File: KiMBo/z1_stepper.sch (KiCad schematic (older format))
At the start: 23 parts, among them U21 TMC2130

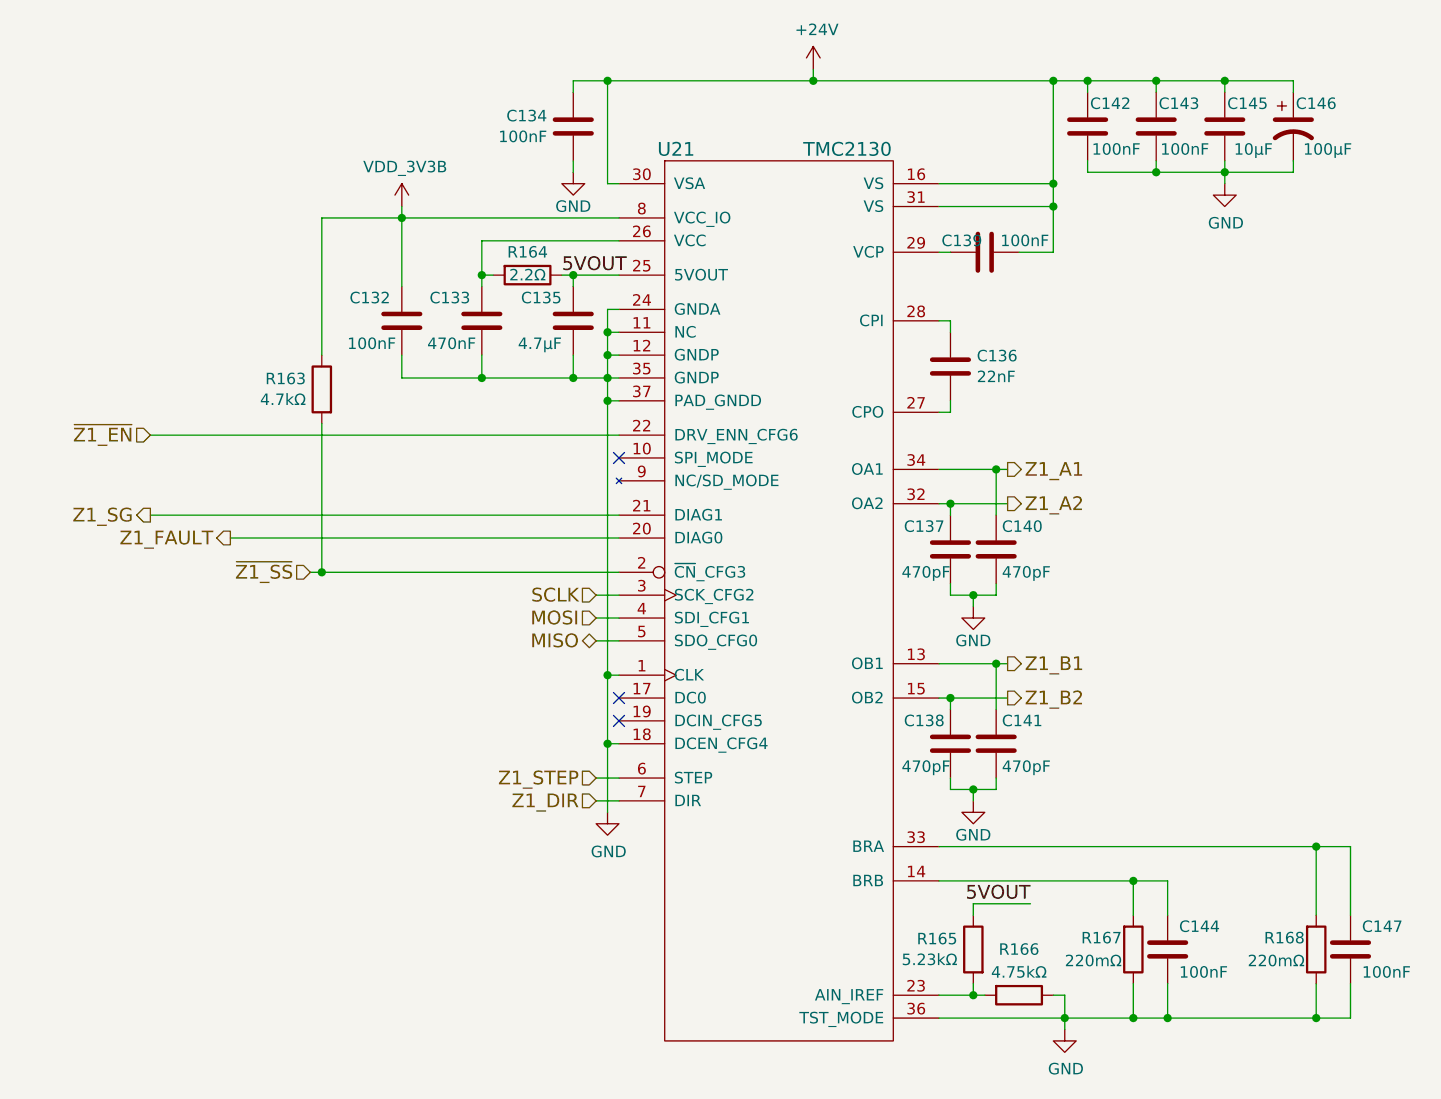
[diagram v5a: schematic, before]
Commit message: Remove HDMI from the schematic
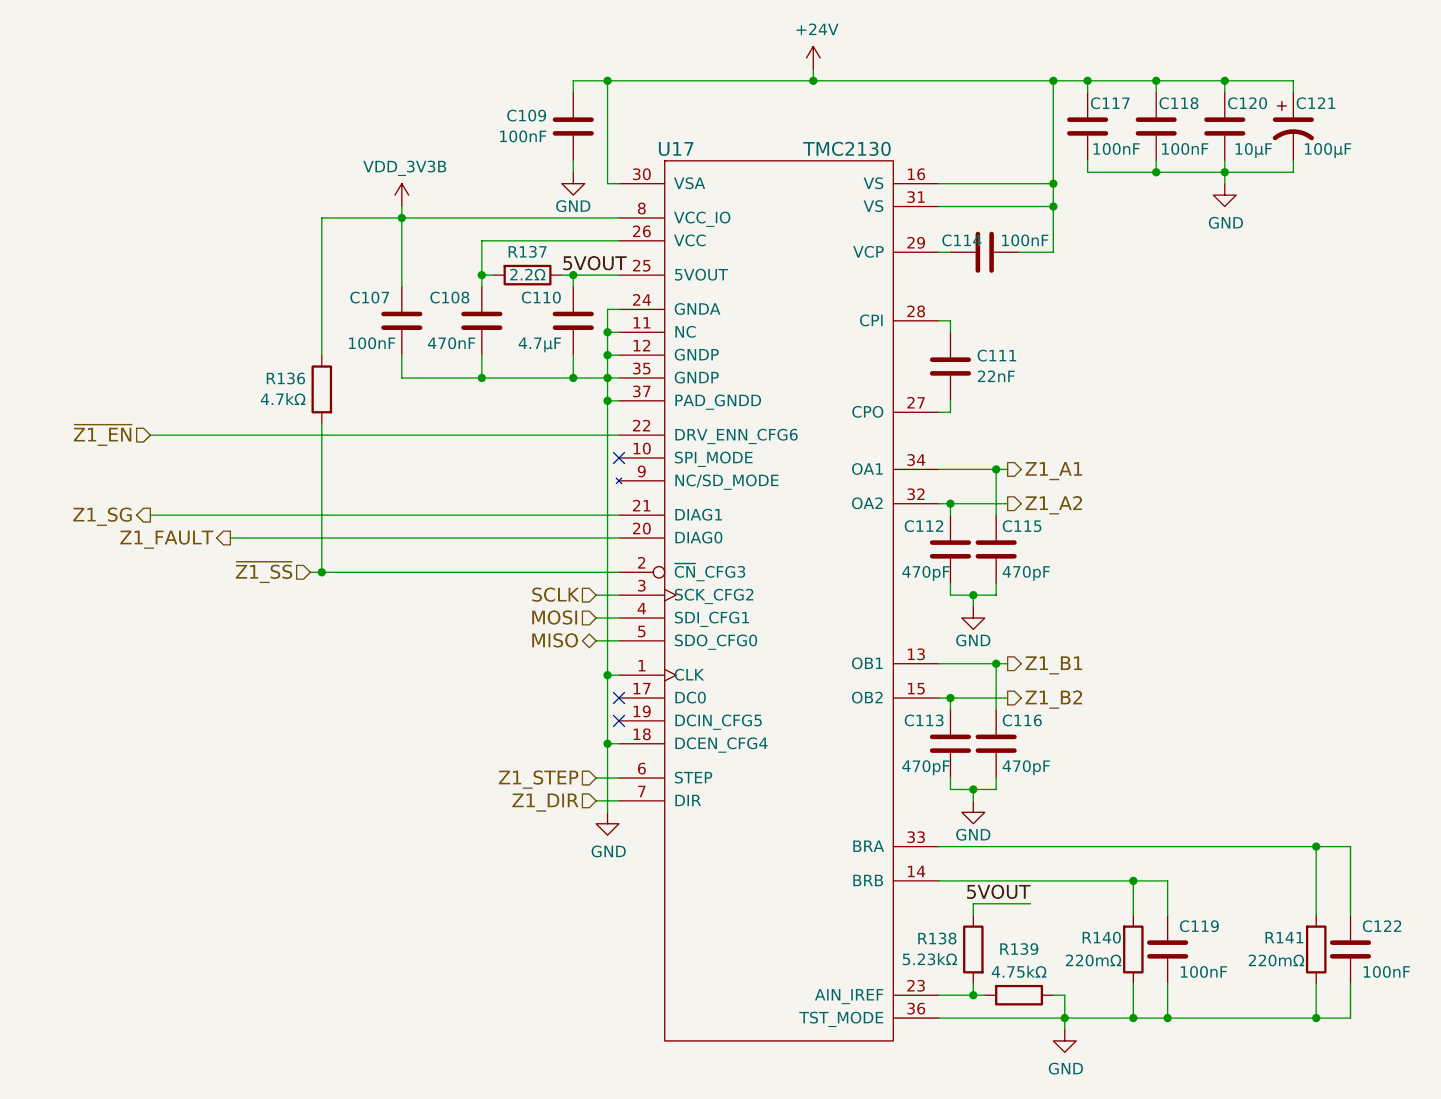
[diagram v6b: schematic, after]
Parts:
- renumbered C132 to C107, C133 to C108, C134 to C109, C135 to C110, C136 to C111, C137 to C112, C138 to C113, C139 to C114, C140 to C115, C141 to C116, C142 to C117, C143 to C118, C144 to C119, C145 to C120, C146 to C121, C147 to C122, R163 to R136, R164 to R137, R165 to R138, R166 to R139, R167 to R140, R168 to R141, U21 to U17
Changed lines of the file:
@@
 $Descr A3 16535 11693
 encoding utf-8
-Sheet 19 26
+Sheet 19 25
 Title ""
 Date ""
@@
 Z1_SG
 $Comp
-L C C134
+L C C109
 U 1 1 58C0CFD1
 P 7400 3050
-F 0 "C134" H 7286 3004 50  0000 R CNN
+F 0 "C109" H 7286 3004 50  0000 R CNN
 F 1 "100nF" H 7286 3095 50  0000 R CNN
 F 2 "Capacitors_SMD:C_0603" H 7438 2900 50  0001 C CNN
@@
 $EndComp
 $Comp
-L C C139
+L C C114
 U 1 1 58C0CFD8
 P 9200 3600
-F 0 "C139" V 9150 3500 50  0000 C CNN
+F 0 "C114" V 9150 3500 50  0000 C CNN
 F 1 "100nF" V 9150 3775 50  0000 C CNN
 F 2 "Capacitors_SMD:C_0603" H 9238 3450 50  0001 C CNN
@@
 $EndComp
 $Comp
-L CP1 C146
+L CP1 C121
 U 1 1 58C0CFDF
 P 10550 3050
-F 0 "C146" H 10650 3150 50  0000 C CNN
+F 0 "C121" H 10650 3150 50  0000 C CNN
 F 1 "100μF" H 10700 2950 50  0000 C CNN
 F 2 "Capacitors_SMD:c_elec_8x10" H 10550 3050 50  0001 C CNN
@@
 $EndComp
 $Comp
-L C C142
+L C C117
 U 1 1 58C0CFE6
 P 9650 3050
-F 0 "C142" H 9550 3150 50  0000 C CNN
+F 0 "C117" H 9550 3150 50  0000 C CNN
 F 1 "100nF" H 9525 2950 50  0000 C CNN
 F 2 "Capacitors_SMD:C_0603" H 9688 2900 50  0001 C CNN
@@
 $EndComp
 $Comp
-L GND #PWR0224
+L GND #PWR0193
 U 1 1 58C0CFED
 P 7400 3250
-F 0 "#PWR0224" H 7400 3000 50  0001 C CNN
+F 0 "#PWR0193" H 7400 3000 50  0001 C CNN
 F 1 "GND" H 7400 3100 50  0000 C CNN
 F 2 "" H 7400 3250 50  0000 C CNN
@@
 $EndComp
 $Comp
-L C C143
+L C C118
 U 1 1 58C0CFF3
 P 9950 3050
-F 0 "C143" H 9850 3150 50  0000 C CNN
+F 0 "C118" H 9850 3150 50  0000 C CNN
 F 1 "100nF" H 9825 2950 50  0000 C CNN
 F 2 "Capacitors_SMD:C_0603" H 9988 2900 50  0001 C CNN
@@
 $EndComp
 $Comp
-L GND #PWR0225
+L GND #PWR0194
 U 1 1 58C0CFFA
 P 10250 3300
-F 0 "#PWR0225" H 10250 3050 50  0001 C CNN
+F 0 "#PWR0194" H 10250 3050 50  0001 C CNN
 F 1 "GND" H 10255 3127 50  0000 C CNN
 F 2 "" H 10250 3300 50  0000 C CNN
@@
 $EndComp
 $Comp
-L +24V #PWR0226
+L +24V #PWR0195
 U 1 1 58C0D000
 P 8450 2800
-F 0 "#PWR0226" H 8450 2650 50  0001 C CNN
+F 0 "#PWR0195" H 8450 2650 50  0001 C CNN
 F 1 "+24V" H 8465 2973 50  0000 C CNN
 F 2 "" H 8450 2800 50  0000 C CNN
@@
 $EndComp
 $Comp
-L C C136
+L C C111
 U 1 1 58C0D006
 P 9050 4100
-F 0 "C136" H 9165 4146 50  0000 L CNN
+F 0 "C111" H 9165 4146 50  0000 L CNN
 F 1 "22nF" H 9165 4055 50  0000 L CNN
 F 2 "Capacitors_SMD:C_0603" H 9088 3950 50  0001 C CNN
@@
 $EndComp
 $Comp
-L R R168
+L R R141
 U 1 1 58C0D00D
 P 10650 6650
-F 0 "R168" H 10600 6600 50  0000 R CNN
+F 0 "R141" H 10600 6600 50  0000 R CNN
 F 1 "220mΩ" H 10600 6700 50  0000 R CNN
 F 2 "Resistors_SMD:R_0805" V 10580 6650 50  0001 C CNN
@@
 $EndComp
 $Comp
-L R R167
+L R R140
 U 1 1 58C0D014
 P 9850 6650
-F 0 "R167" H 9800 6600 50  0000 R CNN
+F 0 "R140" H 9800 6600 50  0000 R CNN
 F 1 "220mΩ" H 9800 6700 50  0000 R CNN
 F 2 "Resistors_SMD:R_0805" V 9780 6650 50  0001 C CNN
@@
 $EndComp
 $Comp
-L GND #PWR0227
+L GND #PWR0196
 U 1 1 58C0D01B
 P 9550 7000
-F 0 "#PWR0227" H 9550 6750 50  0001 C CNN
+F 0 "#PWR0196" H 9550 6750 50  0001 C CNN
 F 1 "GND" H 9555 6827 50  0000 C CNN
 F 2 "" H 9550 7000 50  0000 C CNN
@@
 NoConn ~ 7600 5550
 $Comp
-L R R164
+L R R137
 U 1 1 58C0D022
 P 7200 3700
-F 0 "R164" V 7100 3700 50  0000 C CNN
+F 0 "R137" V 7100 3700 50  0000 C CNN
 F 1 "2.2Ω" V 7200 3700 50  0000 C CNN
 F 2 "Resistors_SMD:R_0603" V 7130 3700 50  0001 C CNN
@@
 $EndComp
 $Comp
-L C C133
+L C C108
 U 1 1 58C0D029
 P 7000 3900
-F 0 "C133" H 7050 4000 50  0000 L CNN
+F 0 "C108" H 7050 4000 50  0000 L CNN
 F 1 "470nF" H 7025 3800 50  0000 L CNN
 F 2 "Capacitors_SMD:C_0603" H 7038 3750 50  0001 C CNN
@@
 NoConn ~ 7600 5650
 $Comp
-L GND #PWR0228
+L GND #PWR0197
 U 1 1 58C0D03E
 P 7550 6050
-F 0 "#PWR0228" H 7550 5800 50  0001 C CNN
+F 0 "#PWR0197" H 7550 5800 50  0001 C CNN
 F 1 "GND" H 7555 5877 50  0000 C CNN
 F 2 "" H 7550 6050 50  0000 C CNN
@@
 $EndComp
 $Comp
-L C C144
+L C C119
 U 1 1 58C0D044
 P 10000 6650
-F 0 "C144" H 10050 6750 50  0000 L CNN
+F 0 "C119" H 10050 6750 50  0000 L CNN
 F 1 "100nF" H 10050 6550 50  0000 L CNN
 F 2 "Capacitors_SMD:C_0603" H 10038 6500 50  0001 C CNN
@@
 NoConn ~ 7600 4500
 $Comp
-L C C135
+L C C110
 U 1 1 58C0D056
 P 7400 3900
-F 0 "C135" H 7450 4000 50  0000 L CNN
+F 0 "C110" H 7450 4000 50  0000 L CNN
 F 1 "4.7μF" H 7450 3800 50  0000 L CNN
 F 2 "Capacitors_SMD:C_0603" H 7438 3750 50  0001 C CNN
@@
 5VOUT
 $Comp
-L R R165
+L R R138
 U 1 1 58C0D05E
 P 9150 6650
-F 0 "R165" H 9219 6696 50  0000 L CNN
+F 0 "R138" H 9219 6696 50  0000 L CNN
 F 1 "5.23kΩ" H 9219 6605 50  0000 L CNN
 F 2 "Resistors_SMD:R_0603" V 9080 6650 50  0001 C CNN
@@
 5VOUT
 $Comp
-L R R166
+L R R139
 U 1 1 58C0D066
 P 9350 6850
-F 0 "R166" V 9150 6850 50  0000 C CNN
+F 0 "R139" V 9150 6850 50  0000 C CNN
 F 1 "4.75kΩ" V 9250 6850 50  0000 C CNN
 F 2 "Resistors_SMD:R_0603" V 9280 6850 50  0001 C CNN
@@
 $EndComp
 $Comp
-L R R163
+L R R136
 U 1 1 58C0D06D
 P 6300 4200
-F 0 "R163" H 6369 4246 50  0000 L CNN
+F 0 "R136" H 6369 4246 50  0000 L CNN
 F 1 "4.7kΩ" H 6369 4155 50  0000 L CNN
 F 2 "Resistors_SMD:R_0603" V 6230 4200 50  0001 C CNN
@@
 $EndComp
 $Comp
-L C C147
+L C C122
 U 1 1 58C0D074
 P 10800 6650
-F 0 "C147" H 10850 6750 50  0000 L CNN
+F 0 "C122" H 10850 6750 50  0000 L CNN
 F 1 "100nF" H 10850 6550 50  0000 L CNN
 F 2 "Capacitors_SMD:C_0603" H 10838 6500 50  0001 C CNN
@@
 $EndComp
 $Comp
-L C C137
+L C C112
 U 1 1 58C0D07B
 P 9050 4900
-F 0 "C137" H 9075 5000 50  0000 L CNN
+F 0 "C112" H 9075 5000 50  0000 L CNN
 F 1 "470pF" H 9050 4800 50  0000 L CNN
 F 2 "Capacitors_SMD:C_0603" H 9088 4750 50  0001 C CNN
@@
 $EndComp
 $Comp
-L GND #PWR0229
+L GND #PWR0198
 U 1 1 58C0D082
 P 9150 5150
-F 0 "#PWR0229" H 9150 4900 50  0001 C CNN
+F 0 "#PWR0198" H 9150 4900 50  0001 C CNN
 F 1 "GND" H 9150 5000 50  0000 C CNN
 F 2 "" H 9150 5150 50  0000 C CNN
@@
 $EndComp
 $Comp
-L C C140
+L C C115
 U 1 1 58C0D088
 P 9250 4900
-F 0 "C140" H 9275 5000 50  0000 L CNN
+F 0 "C115" H 9275 5000 50  0000 L CNN
 F 1 "470pF" H 9275 4800 50  0000 L CNN
 F 2 "Capacitors_SMD:C_0603" H 9288 4750 50  0001 C CNN
@@
 $EndComp
 $Comp
-L C C138
+L C C113
 U 1 1 58C0D08F
 P 9050 5750
-F 0 "C138" H 9075 5850 50  0000 L CNN
+F 0 "C113" H 9075 5850 50  0000 L CNN
 F 1 "470pF" H 9050 5650 50  0000 L CNN
 F 2 "Capacitors_SMD:C_0603" H 9088 5600 50  0001 C CNN
@@
 $EndComp
 $Comp
-L GND #PWR0230
+L GND #PWR0199
 U 1 1 58C0D096
 P 9150 6000
-F 0 "#PWR0230" H 9150 5750 50  0001 C CNN
+F 0 "#PWR0199" H 9150 5750 50  0001 C CNN
 F 1 "GND" H 9150 5850 50  0000 C CNN
 F 2 "" H 9150 6000 50  0000 C CNN
@@
 $EndComp
 $Comp
-L C C141
+L C C116
 U 1 1 58C0D09C
 P 9250 5750
-F 0 "C141" H 9275 5850 50  0000 L CNN
+F 0 "C116" H 9275 5850 50  0000 L CNN
 F 1 "470pF" H 9275 5650 50  0000 L CNN
 F 2 "Capacitors_SMD:C_0603" H 9288 5600 50  0001 C CNN
@@
 $EndComp
 $Comp
-L TMC2130 U21
+L TMC2130 U17
 U 1 1 58C0D0A3
 P 8300 4650
-F 0 "U21" H 7850 6150 60  0000 C CNN
+F 0 "U17" H 7850 6150 60  0000 C CNN
 F 1 "TMC2130" H 8600 6150 60  0000 C CNN
 F 2 "KiMBo:QFN36_5X6" H 8300 4950 60  0001 C CNN
@@
 	9050 5950 9050 5900
 $Comp
-L C C145
+L C C120
 U 1 1 58C0D122
 P 10250 3050
-F 0 "C145" H 10150 3150 50  0000 C CNN
+F 0 "C120" H 10150 3150 50  0000 C CNN
 F 1 "10μF" H 10125 2950 50  0000 C CNN
 F 2 "Capacitors_SMD:C_0805" H 10288 2900 50  0001 C CNN
@@
 	9000 4550 9300 4550
 $Comp
-L VDD_3V3B #PWR0231
+L VDD_3V3B #PWR0200
 U 1 1 5A314607
 P 6650 3400
-F 0 "#PWR0231" H 6650 3250 50  0001 C CNN
+F 0 "#PWR0200" H 6650 3250 50  0001 C CNN
 F 1 "VDD_3V3B" H 6665 3573 50  0000 C CNN
 F 2 "" H 6650 3400 50  0000 C CNN
@@
 $EndComp
 $Comp
-L C C132
+L C C107
 U 1 1 5A89C1CC
 P 6650 3900
-F 0 "C132" H 6700 4000 50  0000 L CNN
+F 0 "C107" H 6700 4000 50  0000 L CNN
 F 1 "100nF" H 6675 3800 50  0000 L CNN
 F 2 "Capacitors_SMD:C_0603" H 6688 3750 50  0001 C CNN

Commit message: More stepper motor driver progress
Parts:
- renumbered R136 to R138, R137 to R139, R138 to R140, R139 to R141, R140 to R142, R141 to R143
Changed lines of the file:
@@
 $Descr A3 16535 11693
 encoding utf-8
-Sheet 19 25
+Sheet 17 25
 Title ""
 Date ""
@@
 $EndComp
 $Comp
-L R R141
+L R R143
 U 1 1 58C0D00D
 P 10650 6650
-F 0 "R141" H 10600 6600 50  0000 R CNN
+F 0 "R143" H 10600 6600 50  0000 R CNN
 F 1 "220mΩ" H 10600 6700 50  0000 R CNN
 F 2 "Resistors_SMD:R_0805" V 10580 6650 50  0001 C CNN
@@
 $EndComp
 $Comp
-L R R140
+L R R142
 U 1 1 58C0D014
 P 9850 6650
-F 0 "R140" H 9800 6600 50  0000 R CNN
+F 0 "R142" H 9800 6600 50  0000 R CNN
 F 1 "220mΩ" H 9800 6700 50  0000 R CNN
 F 2 "Resistors_SMD:R_0805" V 9780 6650 50  0001 C CNN
@@
 NoConn ~ 7600 5550
 $Comp
-L R R137
+L R R139
 U 1 1 58C0D022
 P 7200 3700
-F 0 "R137" V 7100 3700 50  0000 C CNN
+F 0 "R139" V 7100 3700 50  0000 C CNN
 F 1 "2.2Ω" V 7200 3700 50  0000 C CNN
 F 2 "Resistors_SMD:R_0603" V 7130 3700 50  0001 C CNN
@@
 5VOUT
 $Comp
-L R R138
+L R R140
 U 1 1 58C0D05E
 P 9150 6650
-F 0 "R138" H 9219 6696 50  0000 L CNN
+F 0 "R140" H 9219 6696 50  0000 L CNN
 F 1 "5.23kΩ" H 9219 6605 50  0000 L CNN
 F 2 "Resistors_SMD:R_0603" V 9080 6650 50  0001 C CNN
@@
 5VOUT
 $Comp
-L R R139
+L R R141
 U 1 1 58C0D066
 P 9350 6850
-F 0 "R139" V 9150 6850 50  0000 C CNN
+F 0 "R141" V 9150 6850 50  0000 C CNN
 F 1 "4.75kΩ" V 9250 6850 50  0000 C CNN
 F 2 "Resistors_SMD:R_0603" V 9280 6850 50  0001 C CNN
@@
 $EndComp
 $Comp
-L R R136
+L R R138
 U 1 1 58C0D06D
 P 6300 4200
-F 0 "R136" H 6369 4246 50  0000 L CNN
+F 0 "R138" H 6369 4246 50  0000 L CNN
 F 1 "4.7kΩ" H 6369 4155 50  0000 L CNN
 F 2 "Resistors_SMD:R_0603" V 6230 4200 50  0001 C CNN
